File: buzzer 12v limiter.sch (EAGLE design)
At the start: 9 parts, among them Q1 2N2222, Q2 2N2222, Q3 2N652

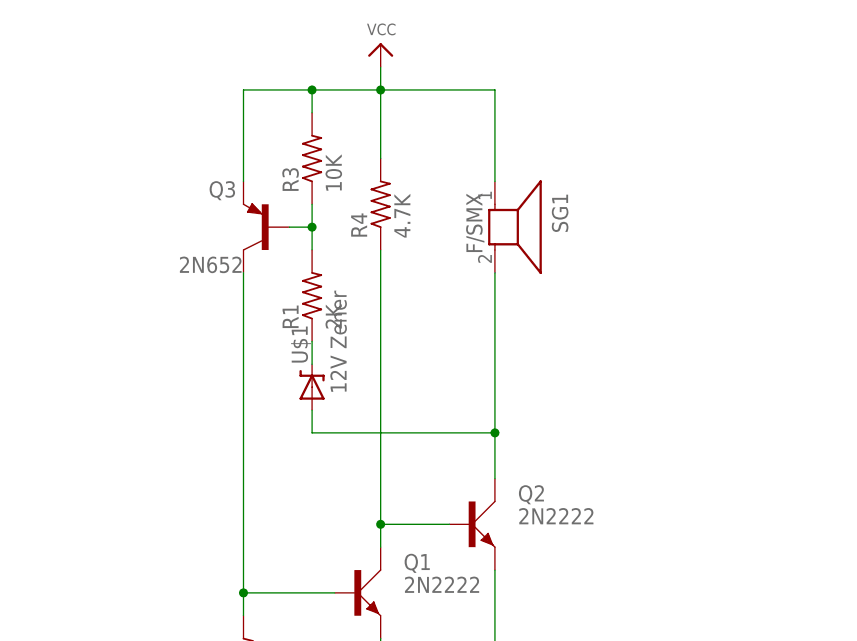
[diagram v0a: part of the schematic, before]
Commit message: Schematics changes
R1 changed to 1K.
C1 10uF capacitor added in parallel to the buzzer
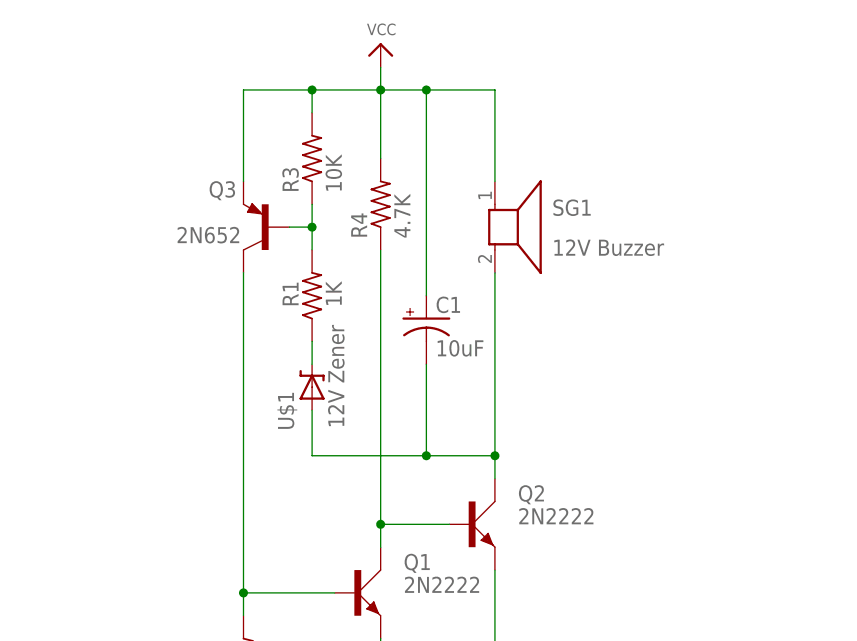
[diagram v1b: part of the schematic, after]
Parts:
- added C1: 10uF, SparkFun-Capacitors:100UF-63V-20%(ELECT)
- R1: value 2K -> 1K
- SG1: value F/SMX -> 12V Buzzer
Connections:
- net N$3: now also C1.-
- net VCC: now also C1.+
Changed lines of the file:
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@@
 <part name="Q1" library="transistor-small-signal" deviceset="2N2222" device=""/>
 <part name="Q2" library="transistor-small-signal" deviceset="2N2222" device=""/>
-<part name="R1" library="adafruit" deviceset="FLIPFLOP-RES" device="" value="2K"/>
+<part name="R1" library="adafruit" deviceset="FLIPFLOP-RES" device="" value="1K"/>
 <part name="R4" library="adafruit" deviceset="FLIPFLOP-RES" device="" value="4.7K"/>
-<part name="SG1" library="buzzer" deviceset="F/SMX" device=""/>
+<part name="SG1" library="buzzer" deviceset="F/SMX" device="" value="12V Buzzer"/>
 <part name="SUPPLY1" library="ATTiny Fuse Reset with 12V Charge Pump" deviceset="GND" device=""/>
 <part name="Q3" library="transistor-pnp" deviceset="2N2907*" device="" value="2N652"/>
@@
 <part name="R3" library="adafruit" deviceset="FLIPFLOP-RES" device="" value="10K"/>
 <part name="P+1" library="ATTiny Fuse Reset with 12V Charge Pump" deviceset="VCC" device=""/>
+<part name="C1" library="SparkFun-Capacitors" deviceset="100UF-63V-20%(ELECT)" device="" value="10uF"/>
 </parts>
 <sheets>
@@
 <instances>
 <instance part="U$1" gate="G$1" x="58.42" y="63.5" smashed="yes" rot="R90">
-<attribute name="NAME" x="57.9374" y="66.04" size="1.778" layer="95" rot="R90"/>
-<attribute name="VALUE" x="62.2554" y="62.738" size="1.778" layer="96" rot="R90"/>
+<attribute name="NAME" x="56.4134" y="58.674" size="1.778" layer="95" rot="R90"/>
+<attribute name="VALUE" x="62.0014" y="58.928" size="1.778" layer="96" rot="R90"/>
 </instance>
 <instance part="Q1" gate="1" x="63.5" y="40.64"/>
 <instance part="Q2" gate="1" x="76.2" y="48.26"/>
-<instance part="R1" gate="G$1" x="58.42" y="73.66" rot="R90"/>
+<instance part="R1" gate="G$1" x="58.42" y="73.66" smashed="yes" rot="R90">
+<attribute name="NAME" x="56.9214" y="72.39" size="1.778" layer="95" rot="R90"/>
+<attribute name="VALUE" x="61.722" y="72.39" size="1.778" layer="96" rot="R90"/>
+</instance>
 <instance part="R4" gate="G$1" x="66.04" y="83.82" rot="R90"/>
-<instance part="SG1" gate="G$1" x="78.74" y="81.28" rot="R270"/>
+<instance part="SG1" gate="G$1" x="78.74" y="81.28" smashed="yes" rot="R270">
+<attribute name="NAME" x="85.09" y="82.55" size="1.778" layer="95"/>
+<attribute name="VALUE" x="85.09" y="78.105" size="1.778" layer="96"/>
+</instance>
 <instance part="SUPPLY1" gate="GND" x="78.74" y="20.32"/>
 <instance part="Q3" gate="G$1" x="53.34" y="81.28" smashed="yes" rot="MR0">
 <attribute name="NAME" x="50.038" y="84.582" size="1.778" layer="95" rot="MR0"/>
-<attribute name="VALUE" x="50.8" y="76.2" size="1.778" layer="96" rot="MR0"/>
+<attribute name="VALUE" x="50.546" y="79.502" size="1.778" layer="96" rot="MR0"/>
 </instance>
 <instance part="R2" gate="G$1" x="50.8" y="33.02" rot="R90"/>
 <instance part="R3" gate="G$1" x="58.42" y="88.9" rot="R90"/>
 <instance part="P+1" gate="VCC" x="66.04" y="101.6"/>
+<instance part="C1" gate="G$1" x="71.12" y="71.12"/>
 </instances>
 <busses>
@@
 <pinref part="SG1" gate="G$1" pin="2"/>
 <pinref part="Q2" gate="1" pin="C"/>
-<wire x1="78.74" y1="76.2" x2="78.74" y2="58.42" width="0.1524" layer="91"/>
+<wire x1="78.74" y1="76.2" x2="78.74" y2="55.88" width="0.1524" layer="91"/>
 <pinref part="U$1" gate="G$1" pin="A"/>
-<wire x1="78.74" y1="58.42" x2="78.74" y2="53.34" width="0.1524" layer="91"/>
-<wire x1="58.42" y1="60.96" x2="58.42" y2="58.42" width="0.1524" layer="91"/>
-<wire x1="58.42" y1="58.42" x2="78.74" y2="58.42" width="0.1524" layer="91"/>
-<junction x="78.74" y="58.42"/>
+<wire x1="78.74" y1="55.88" x2="78.74" y2="53.34" width="0.1524" layer="91"/>
+<wire x1="58.42" y1="60.96" x2="58.42" y2="55.88" width="0.1524" layer="91"/>
+<wire x1="58.42" y1="55.88" x2="71.12" y2="55.88" width="0.1524" layer="91"/>
+<junction x="78.74" y="55.88"/>
+<pinref part="C1" gate="G$1" pin="-"/>
+<wire x1="71.12" y1="55.88" x2="78.74" y2="55.88" width="0.1524" layer="91"/>
+<wire x1="71.12" y1="66.04" x2="71.12" y2="55.88" width="0.1524" layer="91"/>
+<junction x="71.12" y="55.88"/>
 </segment>
 </net>
@@
 <pinref part="R4" gate="G$1" pin="2"/>
 <wire x1="58.42" y1="96.52" x2="66.04" y2="96.52" width="0.1524" layer="91"/>
-<wire x1="66.04" y1="96.52" x2="78.74" y2="96.52" width="0.1524" layer="91"/>
+<wire x1="66.04" y1="96.52" x2="71.12" y2="96.52" width="0.1524" layer="91"/>
+<wire x1="71.12" y1="96.52" x2="78.74" y2="96.52" width="0.1524" layer="91"/>
 <wire x1="66.04" y1="88.9" x2="66.04" y2="96.52" width="0.1524" layer="91"/>
 <wire x1="66.04" y1="96.52" x2="66.04" y2="99.06" width="0.1524" layer="91"/>
@@
 <junction x="58.42" y="96.52"/>
 <pinref part="P+1" gate="VCC" pin="VCC"/>
+<pinref part="C1" gate="G$1" pin="+"/>
+<wire x1="71.12" y1="73.66" x2="71.12" y2="96.52" width="0.1524" layer="91"/>
+<junction x="71.12" y="96.52"/>
 </segment>
 </net>
